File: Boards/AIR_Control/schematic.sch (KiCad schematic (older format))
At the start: 18 parts, among them J1 MicroFit_RA_10, J2 MM_F_VT_20

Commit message: First Pass Air Control Schematic
Need to update buck converter
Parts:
- added C? (x4): C_0.1uF, footprints:C_0805_OEM, symbol Formula:C_0.1uF
- added C?: C_2.2uF, footprints:C_0603_1608Metric, symbol Formula:C_2.2uF
- added C?: C_22uF, footprints:C_1206_OEM, symbol Formula:C_22uF
- added C?: C_33uF, footprints:C_1812_OEM, symbol Formula:C_33uF
- added C?: C_47uF, footprints:C_0805_OEM, symbol Formula:C_47uF
- added C? (x2): C_30pF, footprints:C_0805_OEM, symbol Formula:C_30pF
- added C?: C_100pF, footprints:C_0805_OEM, symbol Formula:C_100pF
- added D? (x10): LED_0805, footprints:LED_0805_OEM, symbol Formula:LED_0805
- added D?: D_Zener_18V, footprints:DO-214AA, symbol Formula:D_Zener_18V
- added F?: F_500mA_16V, footprints:Fuse_1210, symbol Formula:F_500mA_16V
- added L?: L_100uH, formula:L_100uH, symbol Formula:L_100uH
- added Q? (x4): SSM3K333R, footprints:SOT-23F, symbol Formula:SSM3K333R
- added R? (x5): R_1K, footprints:R_0805_OEM, symbol Formula:R_1K
- added R? (x6): R_200, footprints:R_0805_OEM, symbol Formula:R_200
- added R?: R_25K, footprints:R_0805_OEM, symbol Formula:R_25K
- added R? (x6): R_100K, footprints:R_0805_OEM, symbol Formula:R_100K
- added R?: R_0_2512, footprints:R_2512_OEM, symbol Formula:R_0_2512
- added R? (x7): R_10K, footprints:R_0805_OEM, symbol Formula:R_10K
- added U?: TPS560430YF, Package_TO_SOT_SMD:SOT-23-6_Handsoldering, symbol Formula:TPS560430YF
- added U?: MCP2561-E_SN, footprints:SOIC-8_3.9x4.9mm_Pitch1.27mm_OEM, symbol Formula:MCP2561-E_SN
- added U?: ATMEGA16M1, footprints:TQFP-32_7x7mm_Pitch0.8mm, symbol Formula:ATMEGA16M1
- added Y?: Crystal_SMD, footprints:Crystal_SMD_FA238, symbol Formula:Crystal_SMD
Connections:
- net Air+Aux+ is gone; now on net VCC: J1.3
- net Air-Aux+ is gone; now on net VCC: J1.7
- net +12V: now also D?.1 (K), F?.1
- net AIR+LSD: now also U?.26 ((PCINT5/ADC6/INT2/ACMPN1/AMP2-)PB5)
- net CAN_N: now also R?.2, U?.6 (CANL)
- net CAN_P: now also R?.1, U?.7 (CANH)
- net Cooling_Pressure_Sense: now also U?.28 ((PCINT7/ADC4/SCK/PSCOUT0B)PB7)
- net GND: now also C?.1, C?.2, C?.2, C?.2, C?.2, C?.2, C?.2, C?.2, C?.2, C?.2, D?.1 (K), D?.1 (K), D?.1 (K), D?.1 (K), D?.1 (K), D?.1 (K), D?.1 (K), D?.1 (K), D?.1 (K), D?.1 (K), D?.2 (A), Q?.2 (S), Q?.2 (S), Q?.2 (S), Q?.2 (S), R?.2, R?.2, R?.2, R?.2, R?.2, R?.2, U?.2 (GND), U?.2 (VSS), U?.20 (AGND), U?.5 (GND), U?.8 (STBY), Y?.2, Y?.4
- net MISO: now also U?.1 ((PCINT18/PSCIN2/OC1A/MISO_A)PD2)
- net MOSI: now also U?.2 ((PCINT19/TXD/TXLIN/OC0A/~SS~/MOSI_A)PD3)
- net PrechargeCTL: now also U?.24 ((PCINT4/AMP0+)PB4)
- net RESET: now also R?.2, U?.31 ((PCINT24/OCD/~RESET~)PE0)
- net RJ45_LED1: now also U?.8 ((PCINT0/MISO/PSCOUT2A)PB0)
- net RJ45_LED2: now also U?.9 ((PCINT1/MOSI/PSCOUT2B)PB1)
- net SCK: now also U?.12 ((PCINT20/ADC1/RXD/RXLIN/ICP1A/SCK_A)PD4)
- net ShutdownSense_BMS: now also Q?.1 (G), R?.1, R?.1
- net ShutdownSense_HVD_Conn: now also Q?.1 (G), R?.1, R?.1
- net ShutdownSense_IMD: now also Q?.1 (G), R?.1, R?.1
- net ShutdownSense_MainPack: now also Q?.1 (G), R?.1, R?.1
- net VCC: now also C?.1, C?.2, R?.1, R?.1, R?.1, R?.1, R?.1, R?.1, R?.1, R?.1, U?.3 (VDD), U?.4 (VCC)
- net Air+Aux- renamed AIR+Weld_Detect
- net AIR+Weld_Detect: now also R?.1, R?.1
- net Air-Aux- renamed AIR-Weld_Detect
- net AIR-Weld_Detect: now also R?.1, R?.1
- new net: C?.1, U?.1 (CB)
- new net: R?.1, R?.2, U?.3 (FB)
- new net: C?.1, C?.1, F?.2, R?.1, U?.4 (EN), U?.5 (VIN)
- new net: C?.2, L?.1, U?.6 (SW)
- new net: D?.2 (A), R?.2 (x10)
- new net: C?.1, C?.1, C?.1, L?.2, R?.1, R?.2
- new net: C?.1, U?.10 ((PCINT25/OC0B/XTAL1)PE1), Y?.3
- new net: C?.1, U?.11 ((PCINT26/ADC0/XTAL2)PE2), Y?.1
- new net: C?.1, R?.2, U?.19 (AVCC)
- new net AIR+_Weld_Detect: U?.22 ((PCINT14/ADC10/ACMP1)PC6)
- new net AIR-_Weld_Detect: U?.25 ((PCINT15/D2A/AMP2+)PC7)
- new net BMS_Sense: U?.16 ((PCINT2/ADC5/INT1/ACMPN0)PB2)
- new net IMD_Sense: U?.23 ((PCINT3/AMP0-)PB3)
- new net P_LED_1: R?.1, U?.17 ((PCINT12/ADC8/ACMPN3/AMP1-)PC4)
- new net P_LED_2: R?.1, U?.18 ((PCINT13/ADC9/ACMP3/AMP1+)PC5)
- new net SenseConnToHVD: Q?.3 (D), R?.2, U?.27 ((PCINT6/ADC7/PSCOUT1B)PB6)
- new net SenseMainTSConn: Q?.3 (D), R?.2, U?.29 ((PCINT16/PSCOUT0A)PD0)
- new net XCAN_N: U?.4 (RXD), U?.7 ((PCINT11/T1/ICP1B/RXCAN)PC3)
- new net XCAN_P: U?.1 (TXD), U?.6 ((PCINT10/T0/TXCAN)PC2)
- new net ss_BMS: Q?.3 (D), R?.2, U?.3 ((PCINT9/PSCIN1/OC1B/~SS_A~)PC1)
- new net ss_IMD: Q?.3 (D), R?.2, U?.30 ((PCINT8/INT3/PSCOUT1A)PC0)
- no-connect marks 0 -> 6
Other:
- note added: "(5V)"
- note added: "12V Indicator"
- note added: "5V Indicator"
- note added: "Air+ Weld Detection"
- note added: "Air- Weld Detection"
- note added: "BUCK CONVERTER\n"
- note added: "CAN Transceiver"
- note added: "MICROCONTROLLER"
- note added: "Power Flags"
- note added: "Programming LEDs"
- note added: "Shutdown Sensing"

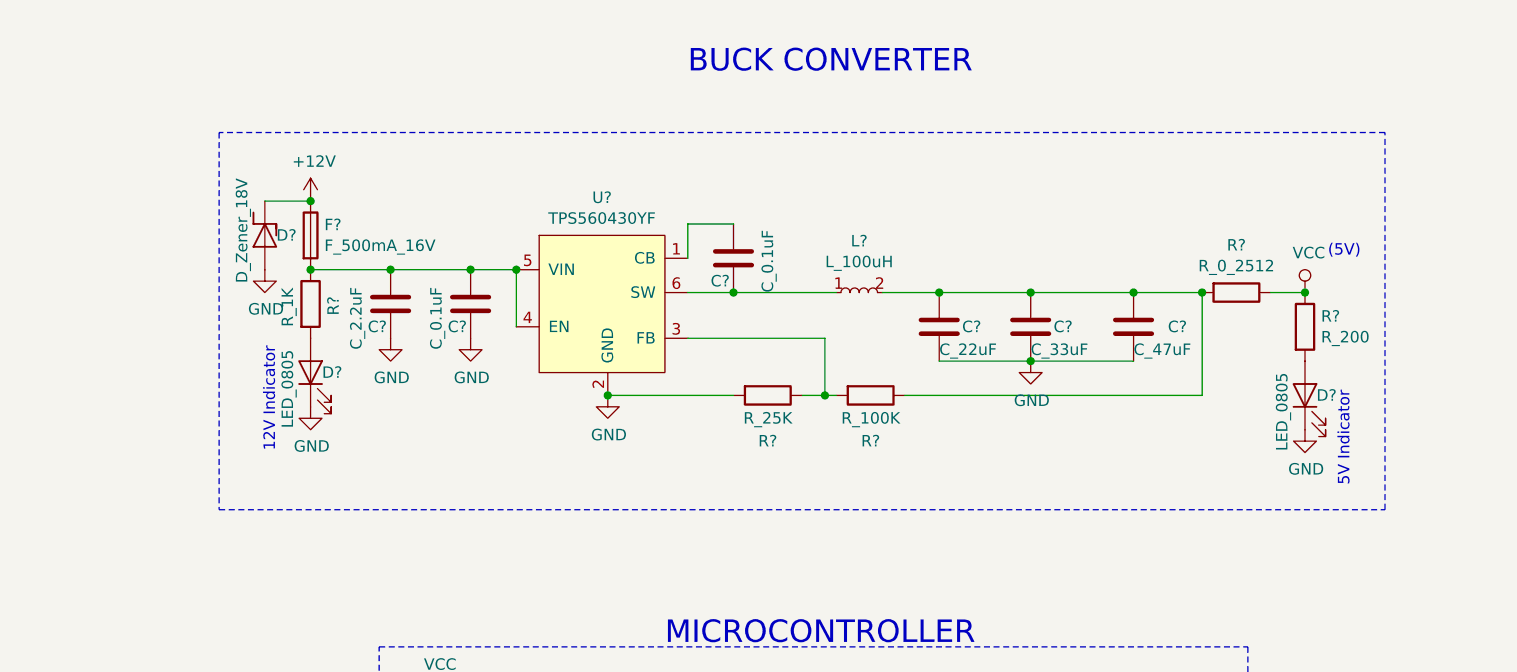
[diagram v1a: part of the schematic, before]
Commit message: First Pass (with updated converter)
Unchecked, but first pass finished with updated buck converted
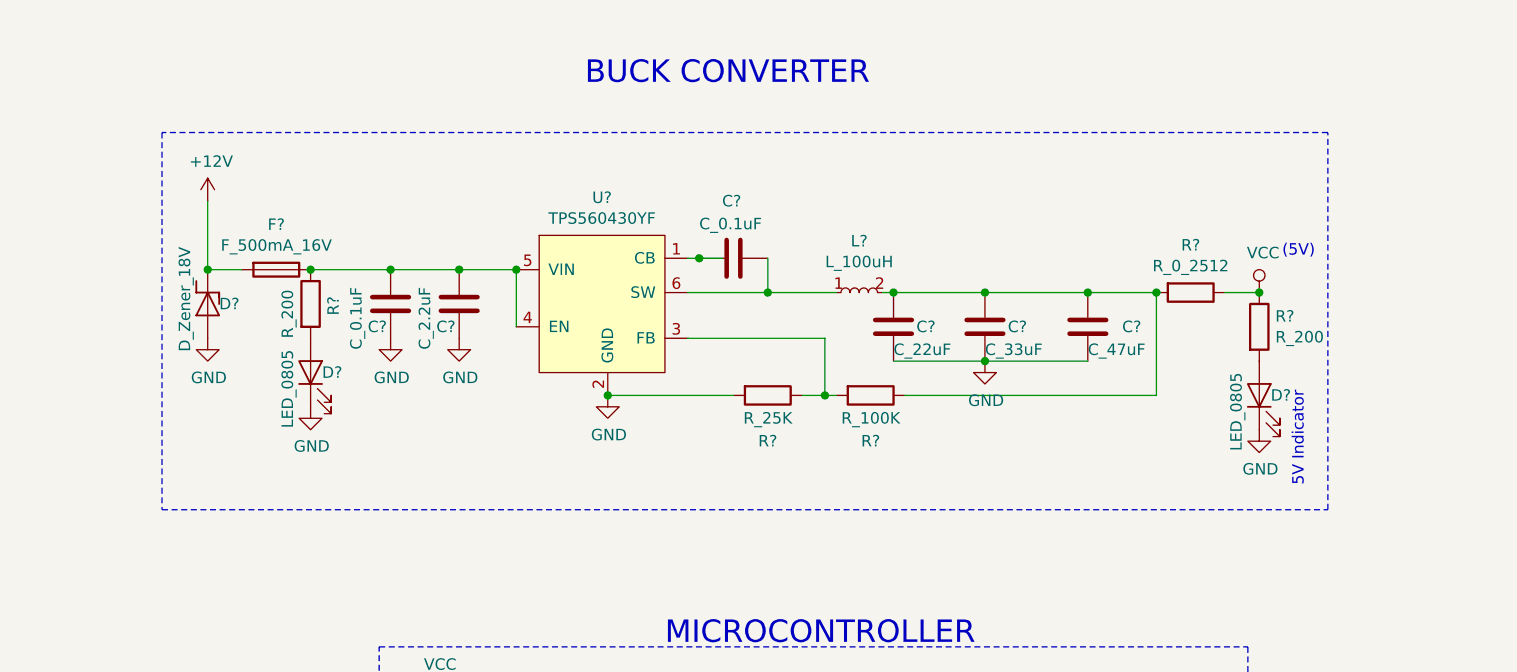
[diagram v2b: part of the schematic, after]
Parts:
- removed F?: F_500mA_16V, footprints:Fuse_1210, symbol Formula:F_500mA_16V
- removed R?: R_1K, footprints:R_0805_OEM, symbol Formula:R_1K
- added F?: F_500mA_16V, footprints:Fuse_1210, symbol Formula:F_500mA_16V
- added R?: R_200, footprints:R_0805_OEM, symbol Formula:R_200
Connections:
- net +12V: now also F?.2
- net at U?.1 (CB): now also C?.2; no longer C?.1
- net at C?.1, C?.1, U?.4 (EN)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: now also F?.1, R?.1
- net at L?.1, U?.6 (SW): now also C?.1; no longer C?.2
- net at D?.2 (A): now also R?.2
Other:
- note removed: "12V Indicator"
- moved on the sheet: C?, D?, R?
